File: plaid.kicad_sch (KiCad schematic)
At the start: 134 parts, among them J1 USB_OTG, J2 AVR_ISP_6, J3 Conn_01x04, J4 GS2, J5 GS2, SW1 SW_Push, SW2 SW_Push, SW3 SW_Push, SW4 SW_Push, SW5 SW_Push, SW6 SW_Push, SW7 SW_Push, SW8 SW_Push, SW9 SW_Push, U1 ATMEGA328-PU, Y1 16MHz

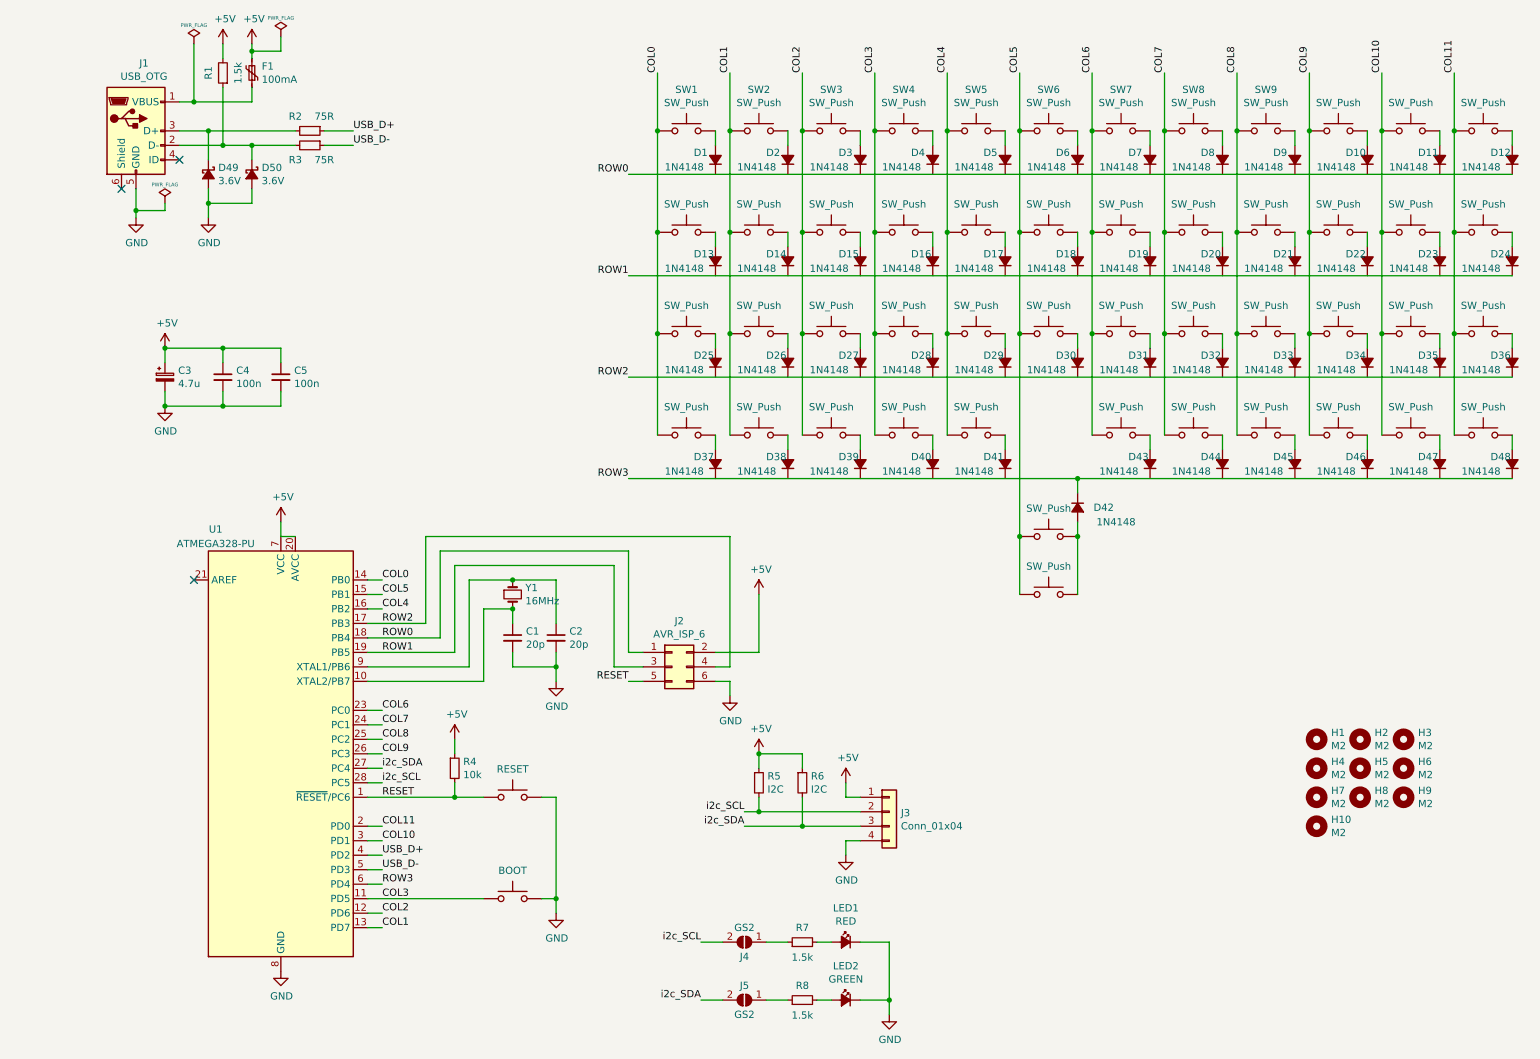
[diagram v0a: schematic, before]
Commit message: Start turning Plaid into Squeezebar
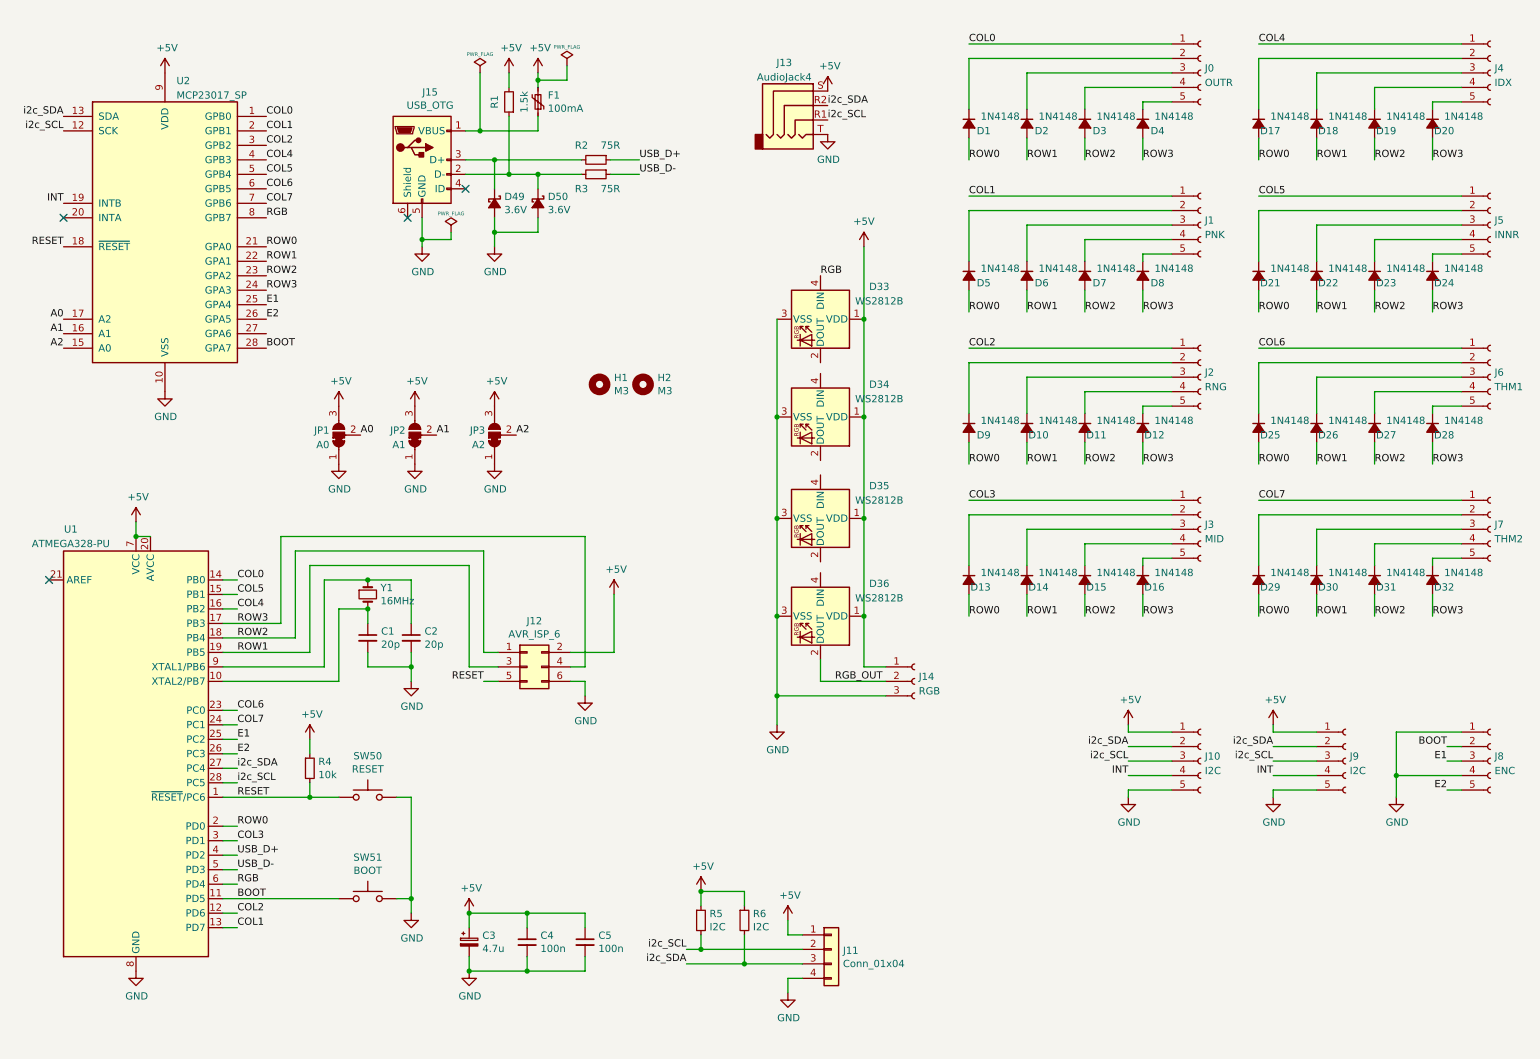
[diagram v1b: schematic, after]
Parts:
- removed ?: SW_Push, SMKJP:SW_Cherry_MX1A_2.0U_PCB_universal_center, symbol Switch:SW_Push
- removed ? (x39), SW1, SW2, SW3, SW4, SW5, SW6, SW7, SW8, SW9: SW_Push, SMKJP:SW_Cherry_MX1A_1.00u_PCB, symbol Switch:SW_Push
- removed D33, D34, D35, D36, D37, D38, D39, D40, D41, D42, D43, D44, D45, D46, D47, D48: 1N4148, dm9_rc:D_DO-35_SOD27_P5.08mm_Horizontal, symbol Device:D_Small_Filled
- removed H10, H3, H4, H5, H6, H7, H8, H9: M2, Mounting_Holes:MountingHole_2.2mm_M2_Pad, symbol Mechanical:MountingHole
- removed J4, J5: GS2, Connectors:GS2, symbol Jumper:SolderJumper_2_Open
- removed LED1: RED, LEDs:LED_D3.0mm, symbol Device:LED_Small_Filled
- removed LED2: GREEN, LEDs:LED_D3.0mm, symbol Device:LED_Small_Filled
- removed R7, R8: 1.5k, Resistors_THT:R_Axial_DIN0204_L3.6mm_D1.6mm_P5.08mm_Horizontal, symbol Device:R_Small
- added D33, D34, D35, D36: WS2812B, LED_SMD:LED_WS2812B_PLCC4_5.0x5.0mm_P3.2mm, symbol LED:WS2812B
- added J0: OUTR, Connector_JST:JST_PH_B5B-PH-K_1x05_P2.00mm_Vertical, symbol Connector:Conn_01x05_Female
- added J1: PNK, Connector_JST:JST_PH_B5B-PH-K_1x05_P2.00mm_Vertical, symbol Connector:Conn_01x05_Female
- added J10, J9: I2C, Connector_JST:JST_PH_B5B-PH-K_1x05_P2.00mm_Vertical, symbol Connector:Conn_01x05_Female
- added J13: AudioJack4, Connector_Audio:Jack_3.5mm_PJ320E_Horizontal, symbol Connector:AudioJack4
- added J14: RGB, Connector_PinSocket_2.54mm:PinSocket_1x03_P2.54mm_Vertical, symbol Connector:Conn_01x03_Female
- added J2: RNG, Connector_JST:JST_PH_B5B-PH-K_1x05_P2.00mm_Vertical, symbol Connector:Conn_01x05_Female
- added J3: MID, Connector_JST:JST_PH_B5B-PH-K_1x05_P2.00mm_Vertical, symbol Connector:Conn_01x05_Female
- added J4: IDX, Connector_JST:JST_PH_B5B-PH-K_1x05_P2.00mm_Vertical, symbol Connector:Conn_01x05_Female
- added J5: INNR, Connector_JST:JST_PH_B5B-PH-K_1x05_P2.00mm_Vertical, symbol Connector:Conn_01x05_Female
- added J6: THM1, Connector_JST:JST_PH_B5B-PH-K_1x05_P2.00mm_Vertical, symbol Connector:Conn_01x05_Female
- added J7: THM2, Connector_JST:JST_PH_B5B-PH-K_1x05_P2.00mm_Vertical, symbol Connector:Conn_01x05_Female
- added J8: ENC, Connector_JST:JST_PH_B5B-PH-K_1x05_P2.00mm_Vertical, symbol Connector:Conn_01x05_Female
- added JP1: A0, Jumper:SolderJumper-3_P1.3mm_Bridged12_Pad1.0x1.5mm, symbol Jumper:SolderJumper_3_Bridged12
- added JP2: A1, Jumper:SolderJumper-3_P1.3mm_Bridged12_Pad1.0x1.5mm, symbol Jumper:SolderJumper_3_Bridged12
- added JP3: A2, Jumper:SolderJumper-3_P1.3mm_Bridged12_Pad1.0x1.5mm, symbol Jumper:SolderJumper_3_Bridged12
- added U2: MCP23017_SP, Package_DIP:DIP-28_W7.62mm, symbol Interface_Expansion:MCP23017_SP
- H1, H2: value M2 -> M3; footprint Mounting_Holes:MountingHole_2.2mm_M2_Pad -> MountingHole:MountingHole_3.2mm_M3
- gave numbers to parts that had none: 2
- renumbered J3 to J11, J2 to J12, J1 to J15
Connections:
- net COL10 is gone; now on net COL3: U1.3 (PD1)
- net COL11 is gone; now on net ROW0: U1.2 (PD0)
- net +5V: now also D33.1 (VDD), D34.1 (VDD), D35.1 (VDD), D36.1 (VDD), J10.1 (Pin_1), J13.S, J14.1 (Pin_1), J9.1 (Pin_1), JP1.3 (B), JP2.3 (B), JP3.3 (B), U2.9 (VDD)
- net COL0: now also J0.1 (Pin_1), U2.1 (GPB0)
- net COL1: now also J1.1 (Pin_1), U2.2 (GPB1)
- net COL2: now also J2.1 (Pin_1), U2.3 (GPB2)
- net COL3: now also J3.1 (Pin_1); no longer SW51.1, U1.11 (PD5)
- net COL4: now also J4.1 (Pin_1), U2.4 (GPB3)
- net COL5: now also J5.1 (Pin_1), U2.5 (GPB4)
- net COL6: now also J6.1 (Pin_1), U2.6 (GPB5)
- net COL7: now also J7.1 (Pin_1), U2.7 (GPB6)
- net GND: now also D33.3 (VSS), D34.3 (VSS), D35.3 (VSS), D36.3 (VSS), J10.5 (Pin_5), J13.T, J14.3 (Pin_3), J8.1 (Pin_1), J8.4 (Pin_4), J9.5 (Pin_5), JP1.1 (A), JP2.1 (A), JP3.1 (A), U2.10 (VSS)
- net RESET: now also U2.18 (~{RESET})
- net ROW0: now also D1.2 (A), D13.2 (A), D17.2 (A), D21.2 (A), D25.2 (A), D29.2 (A), D5.2 (A), D9.2 (A), U2.21 (GPA0); no longer D12.1 (K), J12.1 (Pin_1), U1.18 (PB4)
- net ROW1: now also D10.2 (A), D14.2 (A), D18.2 (A), D2.2 (A), D22.2 (A), D26.2 (A), D30.2 (A), D6.2 (A), U2.22 (GPA1); no longer D24.1 (K)
- net ROW2: now also D11.2 (A), D15.2 (A), D19.2 (A), D23.2 (A), D27.2 (A), D3.2 (A), D31.2 (A), D7.2 (A), J12.1 (Pin_1), U1.18 (PB4), U2.23 (GPA2); no longer J12.4 (Pin_4), U1.17 (PB3)
- net ROW3: now also D12.2 (A), D16.2 (A), D20.2 (A), D24.2 (A), D28.2 (A), D32.2 (A), D4.2 (A), D8.2 (A), J12.4 (Pin_4), U1.17 (PB3), U2.24 (GPA3); no longer U1.6 (PD4)
- net i2c_SCL: now also J10.3 (Pin_3), J13.R1, J9.3 (Pin_3), U2.12 (SCK)
- net i2c_SDA: now also J10.2 (Pin_2), J13.R2, J9.2 (Pin_2), U2.13 (SDA)
- net at D1.1 (K): now also J0.2 (Pin_2)
- net at D13.1 (K): now also J3.2 (Pin_2)
- net at D25.1 (K): now also J6.2 (Pin_2)
- net at D2.1 (K): now also J0.3 (Pin_3)
- net at D14.1 (K): now also J3.3 (Pin_3)
- net at D26.1 (K): now also J6.3 (Pin_3)
- net at D3.1 (K): now also J0.4 (Pin_4)
- net at D15.1 (K): now also J3.4 (Pin_4)
- net at D27.1 (K): now also J6.4 (Pin_4)
- net at D4.1 (K): now also J0.5 (Pin_5)
- net at D16.1 (K): now also J3.5 (Pin_5)
- net at D28.1 (K): now also J6.5 (Pin_5)
- net at D5.1 (K): now also J1.2 (Pin_2)
- net at D17.1 (K): now also J4.2 (Pin_2)
- net at D29.1 (K): now also J7.2 (Pin_2)
- net at D6.1 (K): now also J1.3 (Pin_3)
- net at D18.1 (K): now also J4.3 (Pin_3)
- net at D30.1 (K): now also J7.3 (Pin_3)
- net at D7.1 (K): now also J1.4 (Pin_4)
- net at D19.1 (K): now also J4.4 (Pin_4)
- net at D31.1 (K): now also J7.4 (Pin_4)
- net at D8.1 (K): now also J1.5 (Pin_5)
- net at D20.1 (K): now also J4.5 (Pin_5)
- net at D32.1 (K): now also J7.5 (Pin_5)
- net at D9.1 (K): now also J2.2 (Pin_2)
- net at D21.1 (K): now also J5.2 (Pin_2)
- net at D10.1 (K): now also J2.3 (Pin_3)
- net at D22.1 (K): now also J5.3 (Pin_3)
- net at D11.1 (K): now also J2.4 (Pin_4)
- net at D23.1 (K): now also J5.4 (Pin_4)
- net COL8 renamed E1
- net E1: now also J8.3 (Pin_3), U2.25 (GPA4)
- net COL9 renamed E2
- net E2: now also J8.5 (Pin_5), U2.26 (GPA5)
- new net: D12.1 (K), J2.5 (Pin_5)
- new net: D24.1 (K), J5.5 (Pin_5)
- new net A0: JP1.2 (C), U2.17 (A2)
- new net A1: JP2.2 (C), U2.16 (A1)
- new net A2: JP3.2 (C), U2.15 (A0)
- new net BOOT: J8.2 (Pin_2), SW51.1, U1.11 (PD5), U2.28 (GPA7)
- new net INT: J10.4 (Pin_4), J9.4 (Pin_4), U2.19 (INTB)
- new net RGB: D33.4 (DIN), U1.6 (PD4), U2.8 (GPB7)
- new net RGB_OUT: D36.2 (DOUT), J14.2 (Pin_2)
- no-connect marks 3 -> 4
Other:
- moved on the sheet: C1, C2, C3, C4, C5, D1, D10, D11, D12, D13, D14, D15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

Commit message: Route a Squeezebar
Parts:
- removed D1, D10, D11, D12, D13, D14, D15, D16, D17, D18, D19, D2, D20, D21, D22, D23, D24, D25, D26, D27, D28, D29, D3, D30, D31, D32, D4, D5, D6, D7, D8, D9: 1N4148, dm9_rc:D_DO-35_SOD27_P5.08mm_Horizontal, symbol Device:D_Small_Filled
- removed JP1: A0, Jumper:SolderJumper-3_P1.3mm_Bridged12_Pad1.0x1.5mm, symbol Jumper:SolderJumper_3_Bridged12
- removed JP2: A1, Jumper:SolderJumper-3_P1.3mm_Bridged12_Pad1.0x1.5mm, symbol Jumper:SolderJumper_3_Bridged12
- removed JP3: A2, Jumper:SolderJumper-3_P1.3mm_Bridged12_Pad1.0x1.5mm, symbol Jumper:SolderJumper_3_Bridged12
- H1, H2: value M3 -> M2; footprint MountingHole:MountingHole_3.2mm_M3 -> MountingHole:MountingHole_2.2mm_M2
- renumbered J12 to J_MISSING12, J13 to J_MISSING13
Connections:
- net A0 is gone; now on net +5V: U2.17 (A2)
- net A1 is gone; now on net +5V: U2.16 (A1)
- net A2 is gone; now on net +5V: U2.15 (A0)
- net COL0: now also J8.5 (Pin_5), SW51.1, U1.11 (PD5); no longer U1.14 (PB0)
- net COL1: now also U1.2 (PD0); no longer U1.13 (PD7)
- net COL2: now also U1.3 (PD1); no longer U1.12 (PD6)
- net COL3: now also U1.12 (PD6); no longer U1.3 (PD1)
- net COL6: now also U1.6 (PD4); no longer U1.23 (PC0)
- net COL7: now also U1.14 (PB0); no longer U1.24 (PC1)
- net E2: now also J8.1 (Pin_1); no longer J8.5 (Pin_5)
- net GND: now also J8.2 (Pin_2); no longer J8.1 (Pin_1), J8.4 (Pin_4)
- net INT: now also J10.2 (Pin_2), J9.2 (Pin_2), J_MISSING12.4 (Pin_4), U1.17 (PB3), U2.20 (INTA); no longer J10.4 (Pin_4), J9.4 (Pin_4), U2.19 (INTB)
- net RGB: now also U1.13 (PD7); no longer U1.6 (PD4)
- net ROW0: now also J0.2 (Pin_2), J1.2 (Pin_2), J2.2 (Pin_2), J3.2 (Pin_2), J4.2 (Pin_2), J5.2 (Pin_2), J6.2 (Pin_2), J7.2 (Pin_2), J_MISSING12.1 (Pin_1), U1.18 (PB4); no longer U1.2 (PD0)
- net ROW1: now also J0.3 (Pin_3), J1.3 (Pin_3), J2.3 (Pin_3), J3.3 (Pin_3), J4.3 (Pin_3), J5.3 (Pin_3), J6.3 (Pin_3), J7.3 (Pin_3)
- net ROW2: now also J0.4 (Pin_4), J1.4 (Pin_4), J2.4 (Pin_4), J3.4 (Pin_4), J4.4 (Pin_4), J5.4 (Pin_4), J6.4 (Pin_4), J7.4 (Pin_4), U1.23 (PC0); no longer J_MISSING12.1 (Pin_1), U1.18 (PB4)
- net ROW3: now also J0.5 (Pin_5), J1.5 (Pin_5), J2.5 (Pin_5), J3.5 (Pin_5), J4.5 (Pin_5), J5.5 (Pin_5), J6.5 (Pin_5), J7.5 (Pin_5), J8.4 (Pin_4), U1.24 (PC1); no longer J_MISSING12.4 (Pin_4), U1.17 (PB3)
- net i2c_SCL: now also J10.4 (Pin_4), J11.3 (Pin_3), J9.4 (Pin_4), R6.2; no longer J10.3 (Pin_3), J11.2 (Pin_2), J9.3 (Pin_3), R5.2
- net i2c_SDA: now also J10.3 (Pin_3), J11.2 (Pin_2), J9.3 (Pin_3), R5.2; no longer J10.2 (Pin_2), J11.3 (Pin_3), J9.2 (Pin_2), R6.2
- net at D33.2 (DOUT): now also D34.4 (DIN)
- net at D34.2 (DOUT): now also D35.4 (DIN)
- net at D36.4 (DIN): now also D35.2 (DOUT)
- removed net BOOT: J8.2 (Pin_2), SW51.1, U1.11 (PD5), U2.28 (GPA7)
